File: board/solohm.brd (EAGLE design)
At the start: 99 x 99 mm, 108 parts, among them U1 20, U10 AP2210K-5.0TRG1, U11 RTC-DS1339A, U12 IRDETECTOR-TSOP6X, U2 MC33171, U4 MC33171, U7 HC4051, U8 LD1117, U9 IRDETECTOR-THRU, Y1 32.768KHz

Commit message: here's the v0.1 hardware version, sent this to board house for fab
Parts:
- added R34, R35: 10K, holla:R0603
- IPANEL: value TESTPOINTTHRU -> (none)
- moved GOLD_ORB_SM1 49.8 mm to (61.2, 82.3), turned to 0 degrees
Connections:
- net DISPLAYRESET: now also R35.2
- net GND: now also R35.1
- net THERMOCOUPLECS: now also R34.1
- net V3.3: now also R34.2
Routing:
- net DISPLAYRESET: track 97.0 -> 100.8 mm
- net THERMOCOUPLECS: track 35.6 -> 39.2 mm
- net VPANEL2: track 25.8 -> 24.1 mm
- net V3.3: track 304.9 -> 306.5 mm
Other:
- board text added: "CC-BY-SA"
- board text added: "GND"

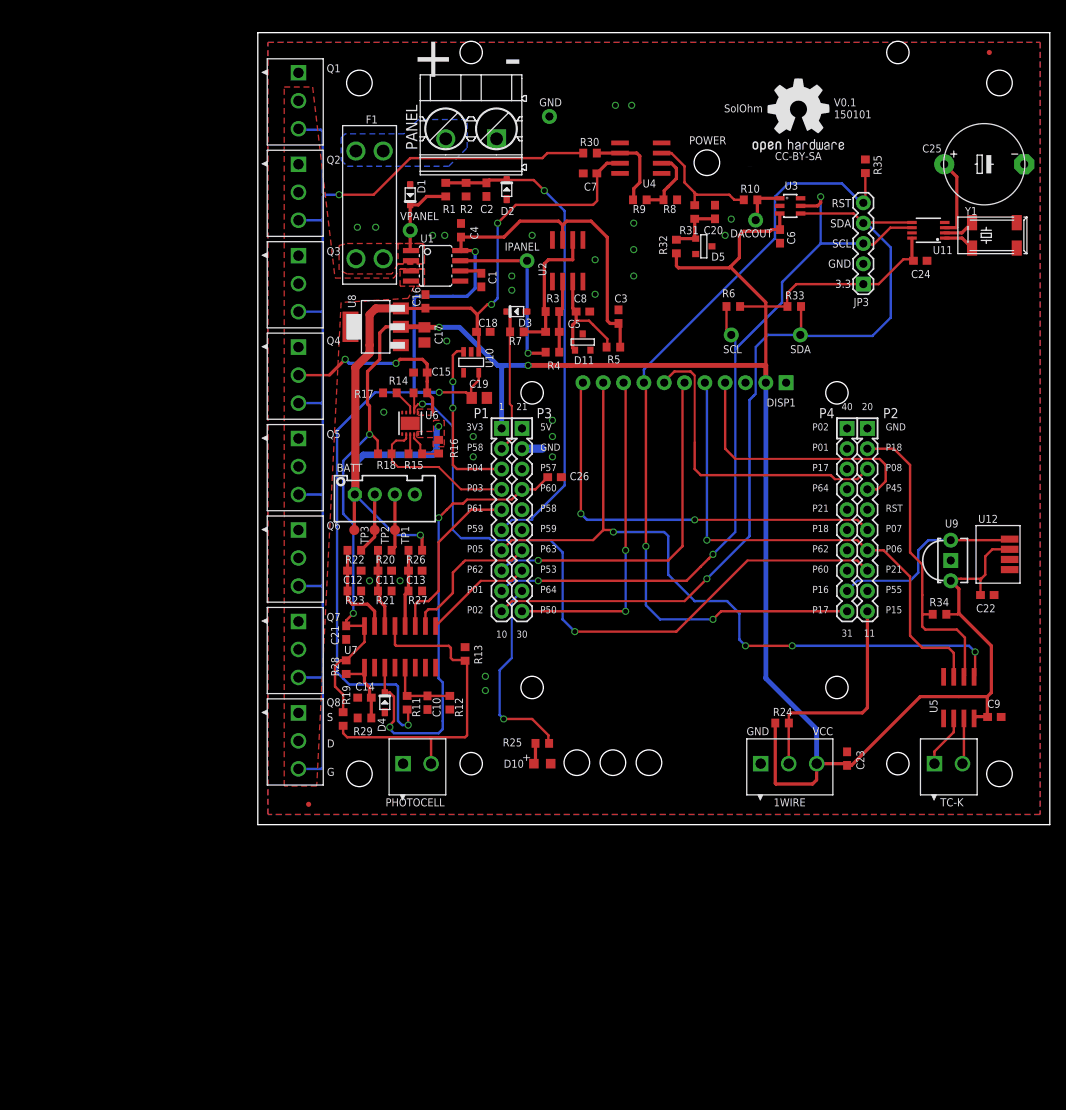
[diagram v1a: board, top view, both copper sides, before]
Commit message: changed top silk char width
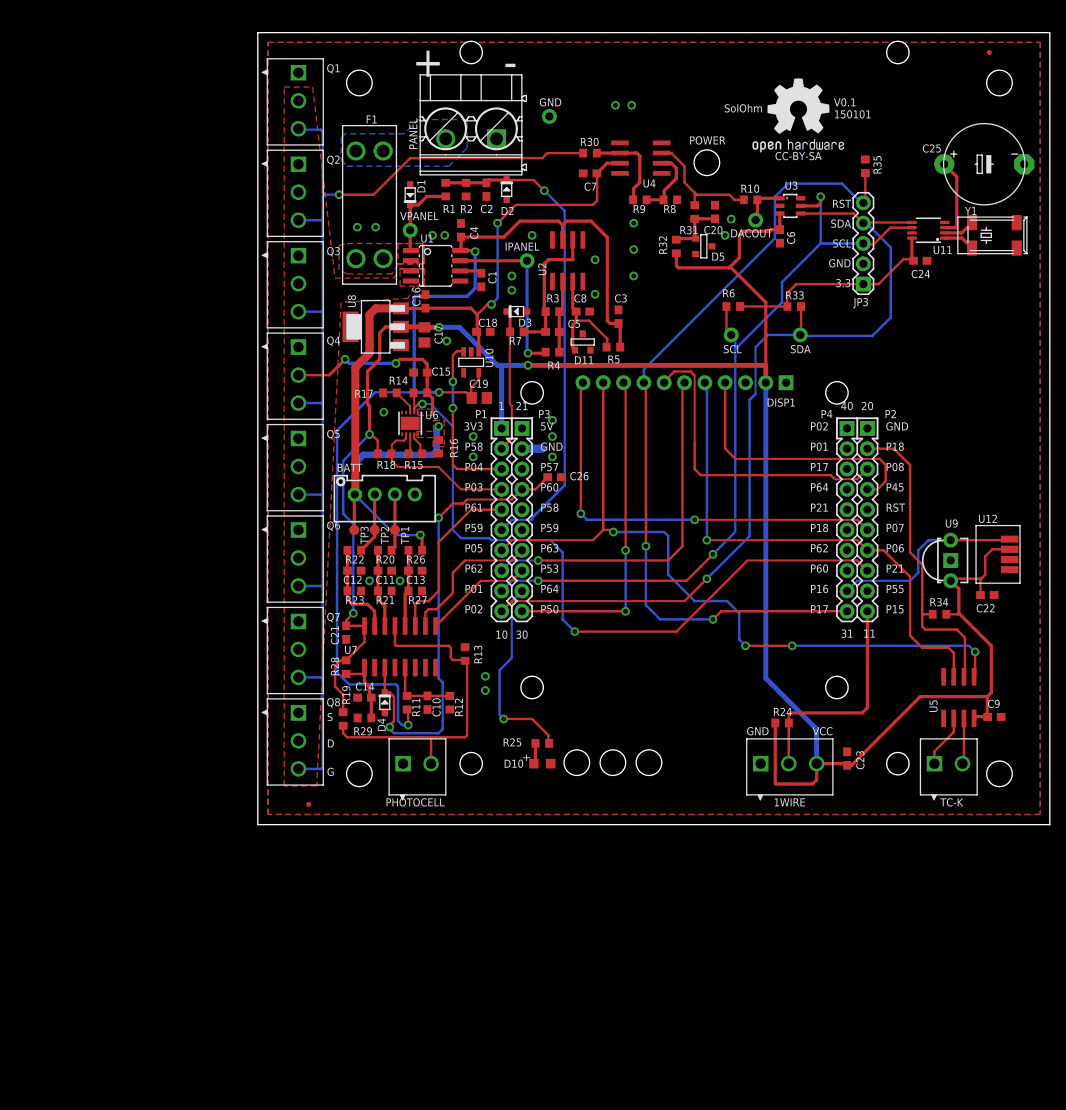
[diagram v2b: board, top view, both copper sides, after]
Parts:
- A1: value (none) -> CC3200-LAUNCHXL-BOOSTERPACK

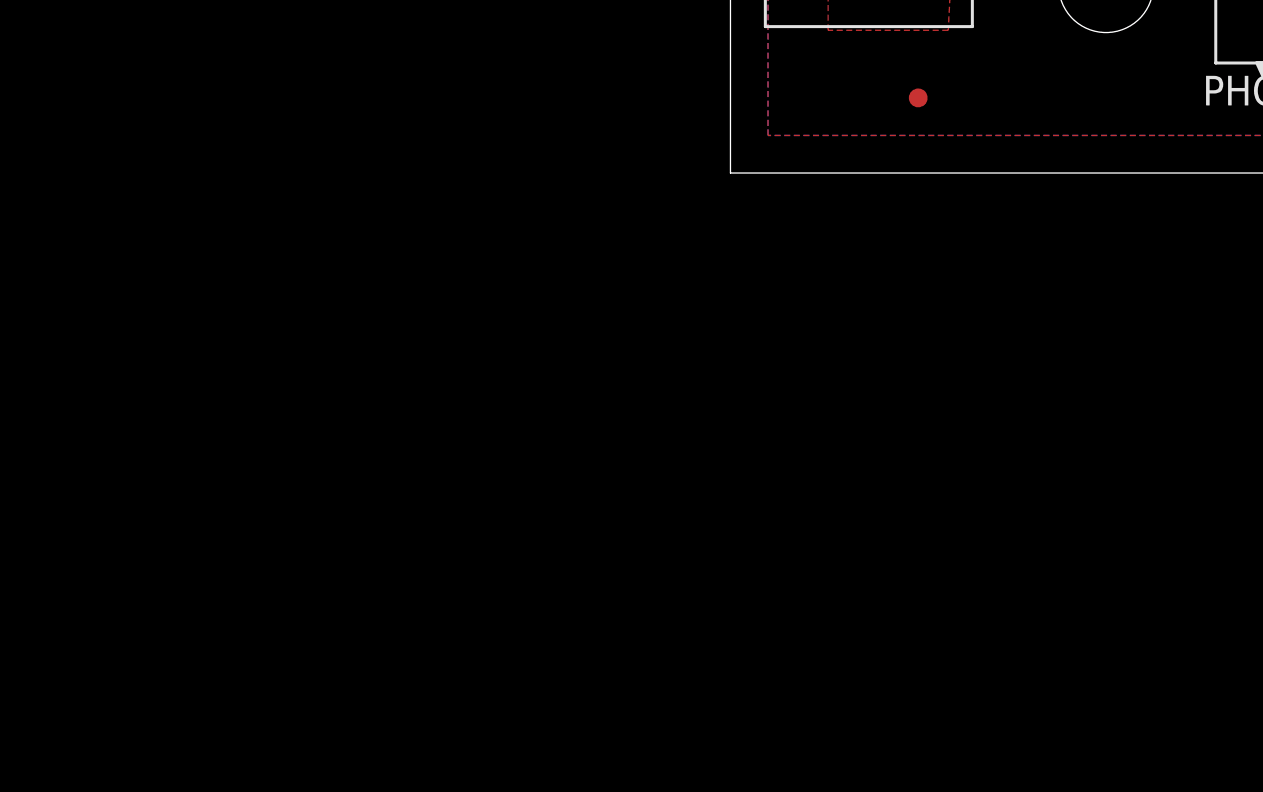
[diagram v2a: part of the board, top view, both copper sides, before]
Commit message: added disconnect for operation in string
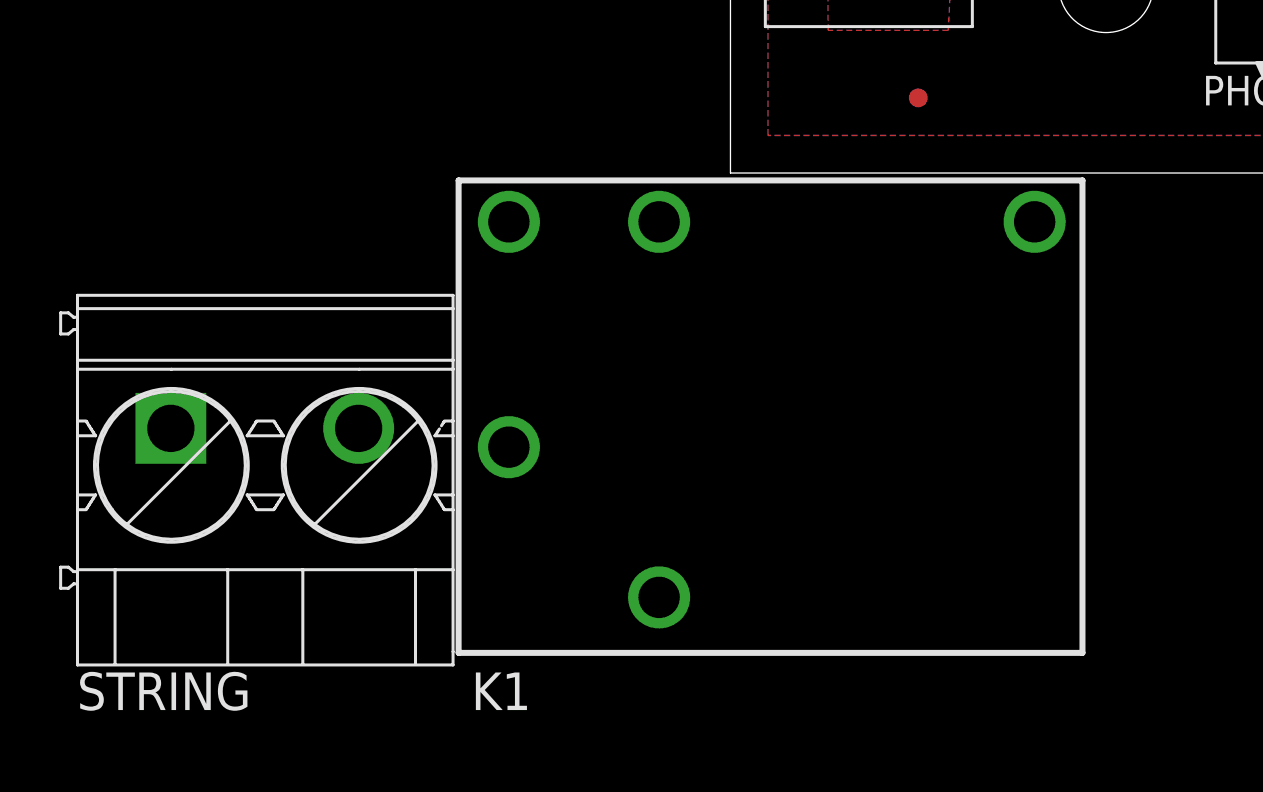
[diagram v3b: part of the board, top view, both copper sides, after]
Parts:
- added K1: (no value), relay:AZ8
- added STRING: (no value), holla:OSTT702
- DACOUT: value TESTPOINTTHRU -> (none)
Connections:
- new net N$20: K1.1, STRING.2
- net GND: now also K1.3, STRING.1
- net VPANEL2: now also K1.4
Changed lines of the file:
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@@
 <attribute name="VALUE" x="34.925" y="8.255" size="1" layer="27" ratio="22"/>
 </element>
-<element name="DACOUT" library="holla" package="TPTHRU" value="TESTPOINTTHRU" x="62.23" y="75.565" smashed="yes" rot="R270">
+<element name="DACOUT" library="holla" package="TPTHRU" value="" x="62.23" y="75.565" smashed="yes" rot="R270">
 <attribute name="DNP" value="1" x="62.23" y="75.565" size="1.778" layer="27" rot="R270" display="off"/>
 <attribute name="NAME" x="59.055" y="73.406" size="1" layer="25" ratio="22"/>
@@
 <attribute name="VALUE" x="74.041" y="82.931" size="1" layer="27" ratio="22" rot="R270"/>
 </element>
+<element name="K1" library="relay" package="AZ8" value="" x="1.397" y="-8.001">
+<attribute name="OC_NEWARK" value="unknown" x="1.397" y="-8.001" size="1.778" layer="27" display="off"/>
+<attribute name="MPN" value="" x="1.397" y="-8.001" size="1.778" layer="27" display="off"/>
+<attribute name="MF" value="" x="1.397" y="-8.001" size="1.778" layer="27" display="off"/>
+<attribute name="OC_FARNELL" value="unknown" x="1.397" y="-8.001" size="1.778" layer="27" display="off"/>
+</element>
+<element name="STRING" library="holla" package="OSTT702" value="" x="-18.923" y="-8.636"/>
 </elements>
 <signals>
@@
 <contactref element="R8" pad="2"/>
 <contactref element="C8" pad="2"/>
-<contactref element="Q1" pad="1"/>
-<contactref element="Q8" pad="1"/>
-<contactref element="Q7" pad="1"/>
-<contactref element="Q6" pad="1"/>
-<contactref element="Q5" pad="1"/>
-<contactref element="Q4" pad="1"/>
-<contactref element="Q3" pad="1"/>
-<contactref element="Q2" pad="1"/>
-<contactref element="R2" pad="1"/>
-<contactref element="C2" pad="2"/>
 <contactref element="PANEL" pad="1"/>
 <contactref element="GND" pad="1"/>
@@
 <contactref element="1WIRE" pad="1"/>
 <contactref element="D10" pad="C"/>
-<contactref element="D2" pad="A"/>
 <contactref element="D3" pad="A"/>
-<contactref element="D1" pad="A"/>
 <contactref element="D11" pad="2"/>
 <contactref element="U6" pad="EXP"/>
@@
 <contactref element="JP3" pad="2"/>
 <contactref element="R35" pad="1"/>
+<contactref element="Q1" pad="1"/>
+<contactref element="Q8" pad="1"/>
+<contactref element="Q7" pad="1"/>
+<contactref element="Q6" pad="1"/>
+<contactref element="Q5" pad="1"/>
+<contactref element="Q4" pad="1"/>
+<contactref element="Q3" pad="1"/>
+<contactref element="Q2" pad="1"/>
+<contactref element="R2" pad="1"/>
+<contactref element="C2" pad="2"/>
+<contactref element="D2" pad="A"/>
+<contactref element="D1" pad="A"/>
+<contactref element="K1" pad="3"/>
+<contactref element="STRING" pad="1"/>
+<wire x1="-7.493" y1="-9.271" x2="-18.923" y2="-8.636" width="0" layer="19" extent="1-1"/>
+<wire x1="5.08" y1="13.97" x2="-7.493" y2="-9.271" width="0" layer="19" extent="1-1"/>
 <wire x1="22.225" y1="19.625" x2="25.908" y2="22.186" width="0" layer="19" extent="1-1"/>
 <wire x1="15.875" y1="14.04" x2="21.209" y2="14.39" width="0" layer="19" extent="1-1"/>
@@
 <vertex x="19.939" y="51.181"/>
 </polygon>
+<contactref element="K1" pad="4"/>
+<wire x1="5.08" y1="10.47" x2="-2.413" y2="-14.351" width="0" layer="19" extent="1-1"/>
+</signal>
+<signal name="N$20">
+<contactref element="K1" pad="1"/>
+<contactref element="STRING" pad="2"/>
+<wire x1="10.287" y1="-1.651" x2="-12.573" y2="-8.636" width="0" layer="19" extent="1-1"/>
 </signal>
 </signals>

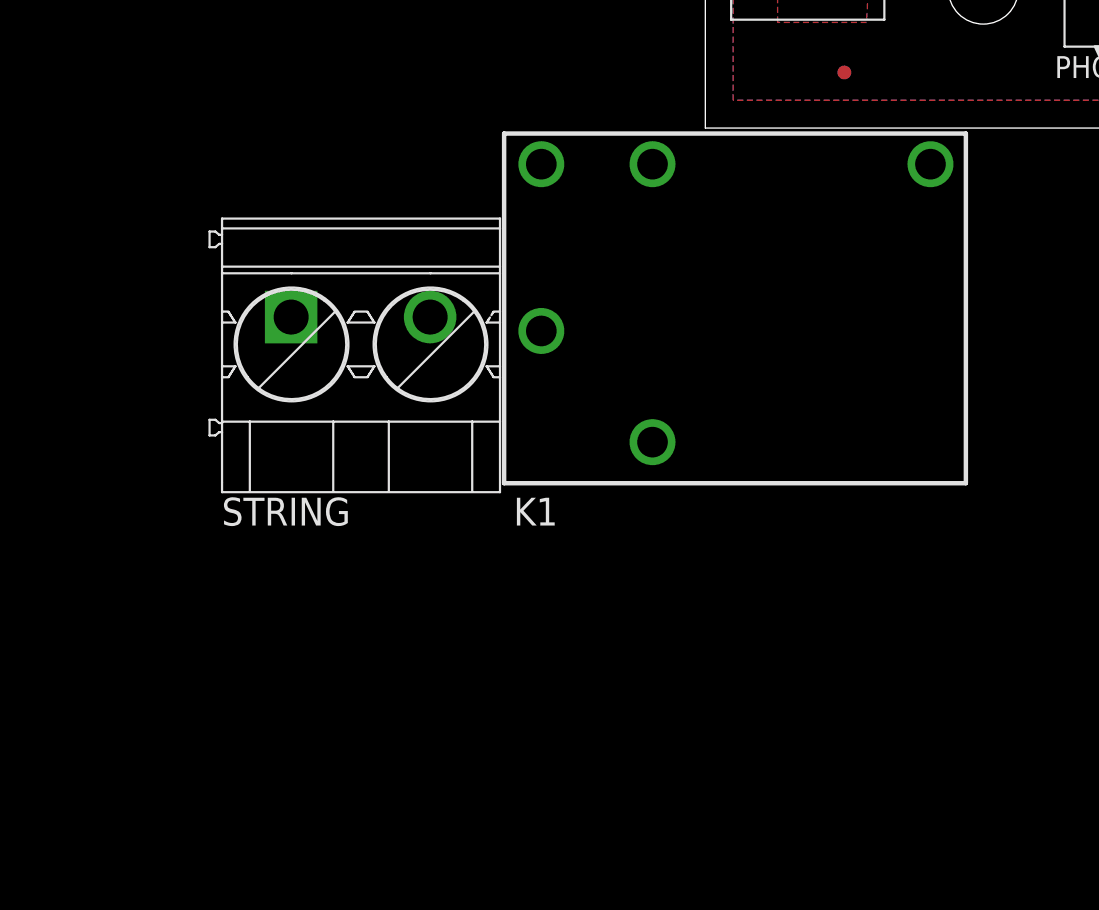
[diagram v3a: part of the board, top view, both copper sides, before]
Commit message: added dual-coil latching relay and 23017 I/O port for future battery charger control
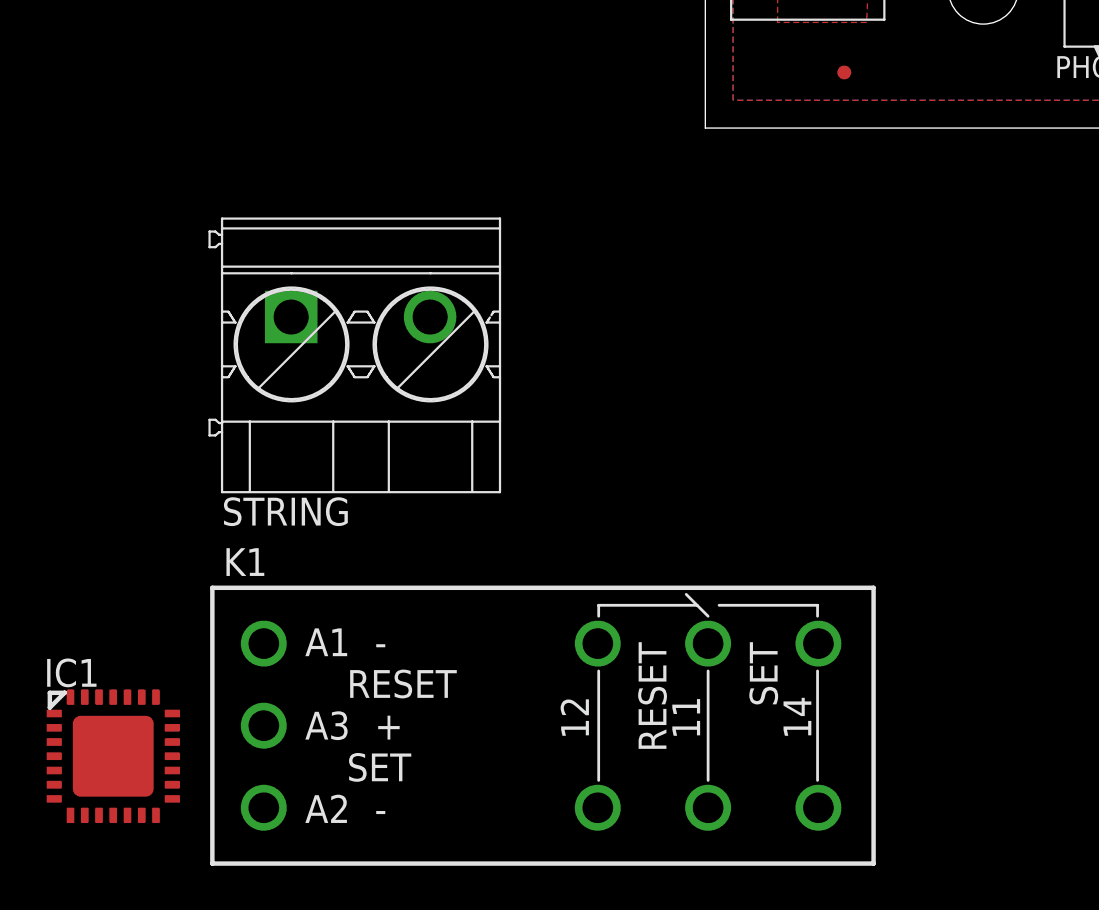
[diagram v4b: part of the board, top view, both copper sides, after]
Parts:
- added IC1: MCP23017ML, microchip:QFN28-ML_6X6MM
- K1: device relay:AZ8 -> holla:RELAY-1FORMC-5MM-16A
- moved K1 19.3 mm to (0.13, -27.3)
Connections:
- removed net DISPLAYRESET: A1.31, DISP1.RESET, JP3.5, R35.2
- new net PERIPHERALRESET: A1.31, DISP1.RESET, IC1.14, JP3.5, R35.2
- net GND: now also IC1.11, IC1.12, IC1.13, IC1.6, K1.14@1, K1.14@2; no longer K1.3
- net I2C_SCL: now also IC1.8
- net I2C_SDA: now also IC1.9
- net N$20: now also K1.11@1, K1.11@2; no longer K1.1
- net V3.3: now also IC1.5
- net VPANEL2: now also K1.12@1, K1.12@2; no longer K1.4
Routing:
- net PERIPHERALRESET: track 0.00 -> 100.8 mm, vias 0 -> 2
- net DISPLAYRESET: track 100.8 -> 0.00 mm, vias 2 -> 0

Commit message: fixed a bunch of top silk errors here and there
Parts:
- removed GOLD_ORB_SM1: LOGO-OSHW_GOLD_ORB_MED, holla:LOGO-OSHW1
- added LOGO1: LOGO-OSHWL, holla:LOGO-OSHW-L
- 1WIRE, Q1, Q2, Q3, Q4, Q5, Q6, Q7, Q8: value (none) -> 1984620
- F1: value (none) -> FUSE-HOLDER-3557-2
- PHOTOCELL: value (none) -> 1984617
- U3: value (none) -> DAC_MCP4725SOT
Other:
- board text removed: "CC-BY-SA"

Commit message: just tweaking things from v0.1 board problems
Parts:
- U6: value (none) -> BATTCHARGER-LTC4079
- moved LOGO1 0.25 mm to (67.6, 88.9)

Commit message: initial add for src little tweaks to the board added lines to board design notes file
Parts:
- R1: value 33k -> 33K
- Y1: value 32.768KHz -> 32.768KHz-6pF
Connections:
- net 1WIRE renamed ONEWIRE
- net V3.3SCALED renamed V3P3SCALED
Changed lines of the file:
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@@
 <attribute name="VALUE" x="26.035" y="68.707" size="1.016" layer="27" ratio="21" rot="R270"/>
 </element>
-<element name="R1" library="holla" package="R0603" value="33k" x="23.495" y="79.375" smashed="yes" rot="R270">
+<element name="R1" library="holla" package="R0603" value="33K" x="23.495" y="79.375" smashed="yes" rot="R270">
 <attribute name="NAME" x="23.114" y="76.454" size="1.016" layer="25" ratio="21"/>
 <attribute name="VALUE" x="21.59" y="80.01" size="1.016" layer="27" ratio="21" rot="R270"/>
@@
 </element>
 <element name="C24" library="holla" package="C0603" value=".1u" x="82.804" y="70.485"/>
-<element name="Y1" library="holla" package="ABS25" value="32.768KHz" x="92.075" y="73.66" smashed="yes">
+<element name="Y1" library="holla" package="ABS25" value="32.768KHz-6pF" x="92.075" y="73.66" smashed="yes">
 <attribute name="NAME" x="88.392" y="76.2" size="1.016" layer="25" ratio="21"/>
 <attribute name="VALUE" x="88.392" y="69.85" size="1.016" layer="27" ratio="21"/>
@@
 <wire x1="84.367" y1="26.289" x2="83.058" y2="26.289" width="0.3048" layer="1"/>
 </signal>
-<signal name="1WIRE">
+<signal name="ONEWIRE">
 <contactref element="1WIRE" pad="2"/>
 <contactref element="R24" pad="1"/>
@@
 <wire x1="18.415" y1="28.79" x2="18.835" y2="29.21" width="0.4064" layer="1"/>
 </signal>
-<signal name="V3.3SCALED">
+<signal name="V3P3SCALED">
 <contactref element="U7" pad="1"/>
 <contactref element="R28" pad="1"/>
